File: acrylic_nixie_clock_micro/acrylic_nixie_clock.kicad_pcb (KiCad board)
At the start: 2 copper layers, 143 x 50 mm, 104 parts, among them IC1 OPT3001DNPR, J1 USB_B_Micro, J2 AVR-ISP-6, Q1 S9013, SW1 SW_Push, SW2 SW_Push, SW3 SW_Push, SW4 SW_Push, U1 ATmega328P-AU, U2 AMS1117-3.3v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

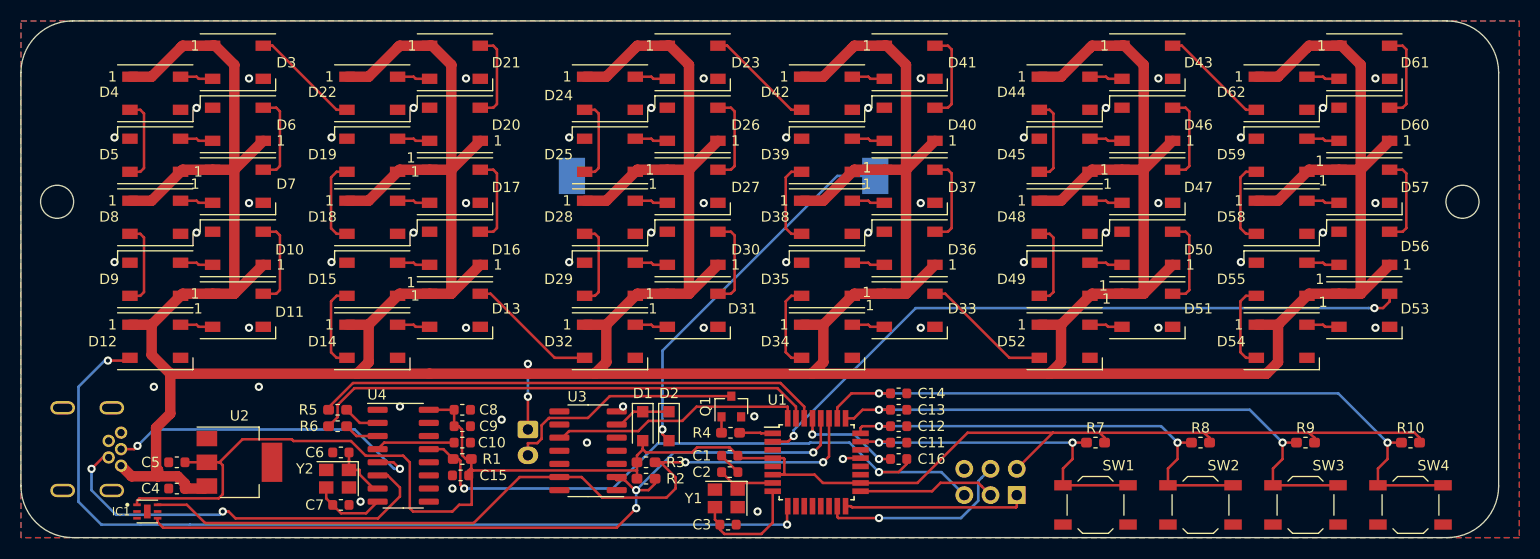
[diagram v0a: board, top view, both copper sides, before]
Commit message: 問題点を修正
CH304Gの電源電圧を3.3Vに
RSTにコンデンサを追加
USBのフットプリントを修正
カードコネクタの追加
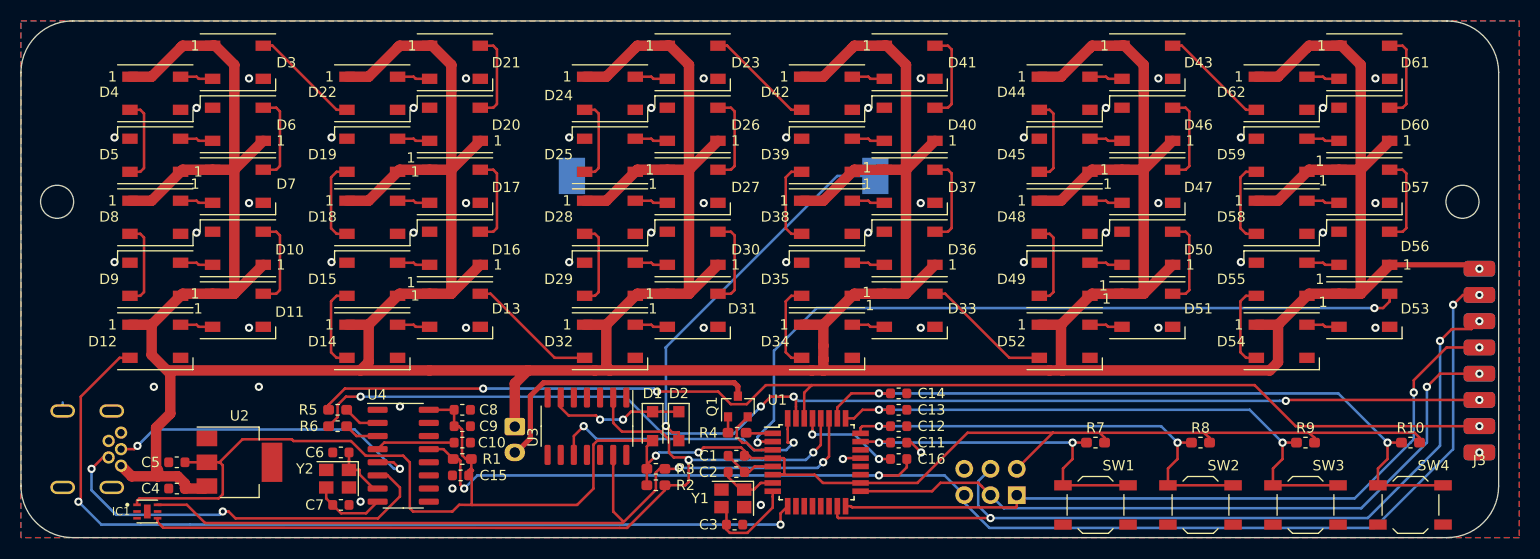
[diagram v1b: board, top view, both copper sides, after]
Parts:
- added J3: Conn_01x08_Female, write_card:writer_card, F.Cu at (191.1, 91.8)
- moved U3 2.38 mm to (104.8, 89.2), turned to 270 degrees
- moved LS1 1.30 mm to (97.8, 89.3)
- moved R2 1.14 mm to (111.4, 94.9)
- moved R3 1.14 mm to (111.4, 93.3)
- moved D1 0.95 mm to (111.1, 89.2)
- moved D2 0.95 mm to (113.7, 89.2)
- moved C1 0.64 mm to (119.2, 92.1)
- moved C2 0.64 mm to (119.2, 93.7)
- moved C3 0.64 mm to (119.1, 98.7)
- moved Y1 0.64 mm to (118.9, 96.2)
- moved Q1 0.63 mm to (119.4, 87.3)
- moved R4 0.63 mm to (119.3, 89.9)
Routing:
- net RXD: track 49.3 -> 119.3 mm, vias 0 -> 3
- net TXD: track 49.3 -> 118.6 mm, vias 0 -> 5
- net RST: track 62.2 -> 129.0 mm, vias 2 -> 4
- net MOSI: track 19.0 -> 82.8 mm, vias 1 -> 3
- net SCK: track 13.4 -> 69.8 mm, vias 0 -> 2
- net MISO: track 17.8 -> 72.1 mm, vias 0 -> 2
- net GND: track 4.88 -> 16.0 mm, vias 53 -> 51
- net +3V3: track 171.6 -> 179.6 mm, vias 0 -> 2
- net Net-(D1-Pad1): track 5.55 -> 13.2 mm, vias 0 -> 2
- net SCL: track 77.0 -> 84.2 mm, vias 3 -> 2
- net DIN: track 66.4 -> 73.4 mm
- net +5V: track 554.2 -> 558.8 mm, vias 2 -> 1
- net Net-(LS1-Pad2): track 23.5 -> 27.9 mm
- net INT: track 24.2 -> 27.7 mm, vias 0 -> 2
- net SDA: track 78.3 -> 80.8 mm
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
